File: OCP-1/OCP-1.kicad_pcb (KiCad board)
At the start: 2 copper layers, 45 x 40 mm, 60 parts, among them K1 кнопка, K2 Кнопка_KLS7-TS5401-1.35-250-T, K3 кнопка, K4 кнопка, K5 кнопка, X1 Клеммник_х2

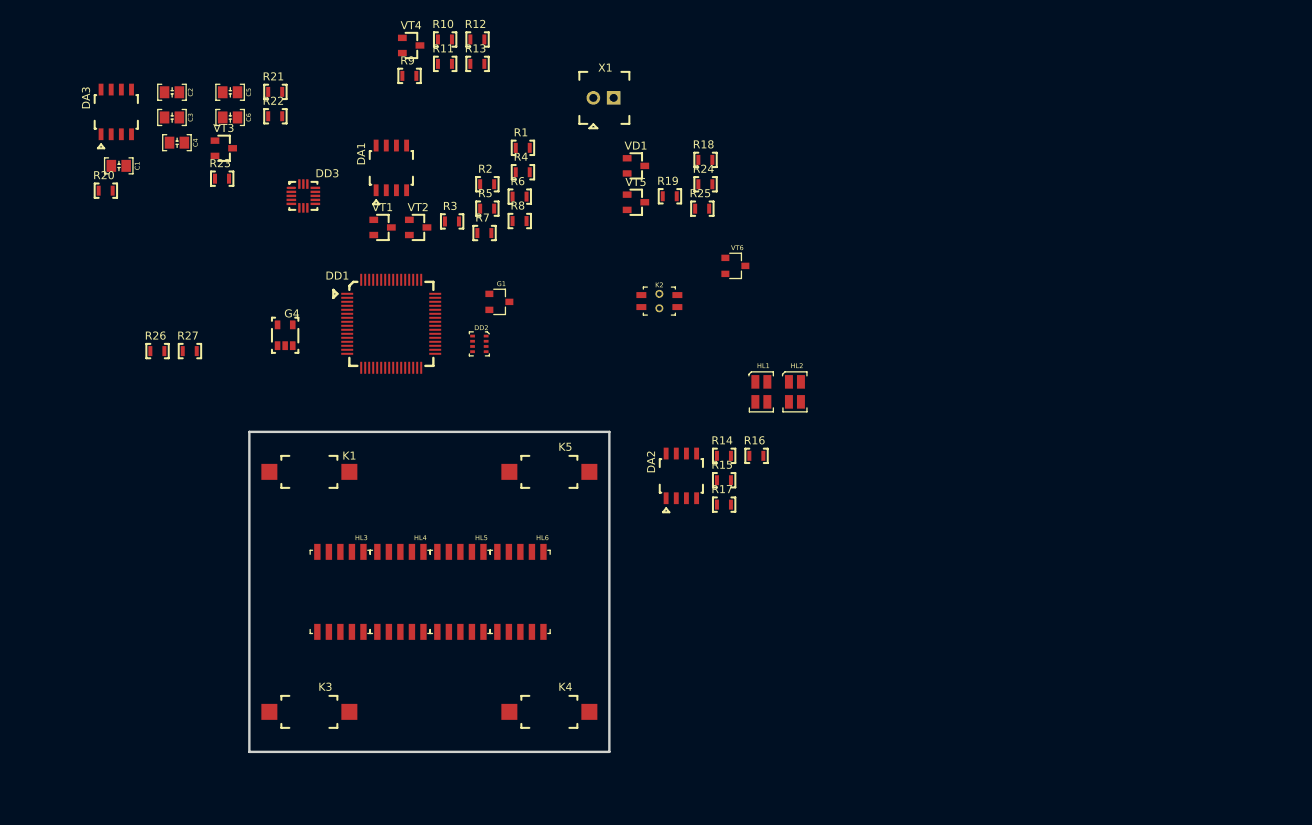
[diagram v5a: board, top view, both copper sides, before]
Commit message: определена схема индикаторов, динамика, не исправлены резисторы питания
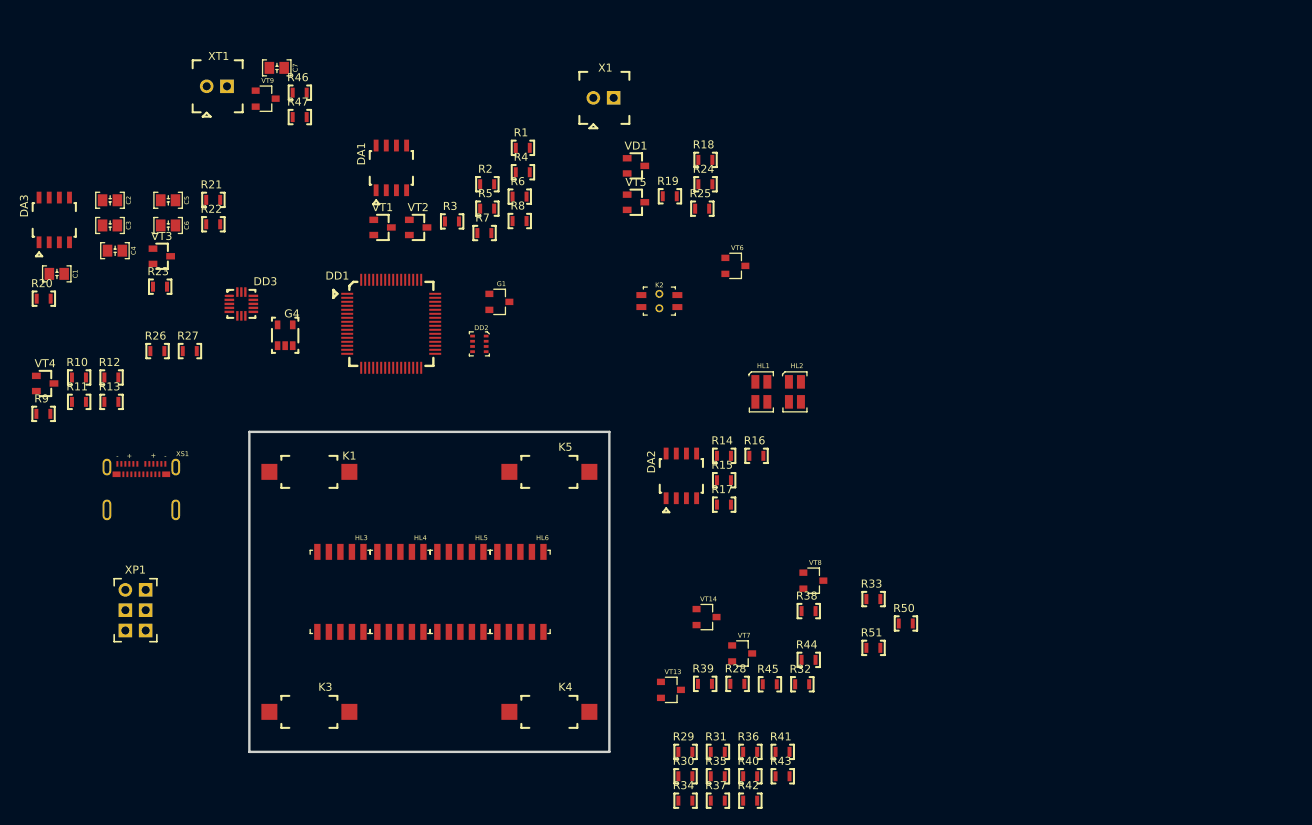
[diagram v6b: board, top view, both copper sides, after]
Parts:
- added C7: Конденсатор_керамический, N_RLC:Конденсатор_SMD_IEC_0805, F.Cu at (77.5, 54.5)
- added R28: Резистор_0,065Вт, N_RLC:Резистор_SMD_0603_0,065_Вт, F.Cu at (136.0, 131.5)
- added R29: Резистор_0,065Вт, N_RLC:Резистор_SMD_0603_0,065_Вт, F.Cu at (129.5, 140.0)
- added R30: Резистор_0,065Вт, N_RLC:Резистор_SMD_0603_0,065_Вт, F.Cu at (129.5, 143.1)
- added R31: Резистор_0,065Вт, N_RLC:Резистор_SMD_0603_0,065_Вт, F.Cu at (133.6, 140.0)
- added R32: Резистор_0,065Вт, N_RLC:Резистор_SMD_0603_0,065_Вт, F.Cu at (144.1, 131.6)
- added R33: Резистор_0,065Вт, N_RLC:Резистор_SMD_0603_0,065_Вт, F.Cu at (153.0, 120.9)
- added R34: Резистор_0,065Вт, N_RLC:Резистор_SMD_0603_0,065_Вт, F.Cu at (129.5, 146.1)
- added R35: Резистор_0,065Вт, N_RLC:Резистор_SMD_0603_0,065_Вт, F.Cu at (133.6, 143.1)
- added R36: Резистор_0,065Вт, N_RLC:Резистор_SMD_0603_0,065_Вт, F.Cu at (137.6, 140.0)
- added R37: Резистор_0,065Вт, N_RLC:Резистор_SMD_0603_0,065_Вт, F.Cu at (133.6, 146.1)
- added R38: Резистор_0,065Вт, N_RLC:Резистор_SMD_0603_0,065_Вт, F.Cu at (144.9, 122.4)
- added R39: Резистор_0,065Вт, N_RLC:Резистор_SMD_0603_0,065_Вт, F.Cu at (131.9, 131.5)
- added R40: Резистор_0,065Вт, N_RLC:Резистор_SMD_0603_0,065_Вт, F.Cu at (137.6, 143.1)
- added R41: Резистор_0,065Вт, N_RLC:Резистор_SMD_0603_0,065_Вт, F.Cu at (141.7, 140.0)
- added R42: Резистор_0,065Вт, N_RLC:Резистор_SMD_0603_0,065_Вт, F.Cu at (137.6, 146.1)
- added R43: Резистор_0,065Вт, N_RLC:Резистор_SMD_0603_0,065_Вт, F.Cu at (141.7, 143.1)
- added R44: Резистор_0,065Вт, N_RLC:Резистор_SMD_0603_0,065_Вт, F.Cu at (144.9, 128.5)
- added R45: Резистор_0,065Вт, N_RLC:Резистор_SMD_0603_0,065_Вт, F.Cu at (140.1, 131.6)
- added R46: Резистор_0,065Вт, N_RLC:Резистор_SMD_0603_0,065_Вт, F.Cu at (81.3, 57.6)
- added R47: Резистор_0,065Вт, N_RLC:Резистор_SMD_0603_0,065_Вт, F.Cu at (81.3, 60.6)
- added R50: Резистор_0,065Вт, N_RLC:Резистор_SMD_0603_0,065_Вт, F.Cu at (157.1, 124.0)
- added R51: Резистор_0,065Вт, N_RLC:Резистор_SMD_0603_0,065_Вт, F.Cu at (153.0, 127.0)
- added VT13: Транзистор_полевой_N-канальный_КП526А9, MOTOR_VD_VT_HL:Корпус_КТ-46, F.Cu at (127.7, 132.2)
- added VT14: Транзистор_полевой_N-канальный_КП526А9, MOTOR_VD_VT_HL:Корпус_КТ-46, F.Cu at (132.1, 123.2)
- added VT7: Транзистор_полевой_N-канальный_КП526А9, MOTOR_VD_VT_HL:Корпус_КТ-46, F.Cu at (136.6, 127.7)
- added VT8: Транзистор_полевой_N-канальный_КП526А9, MOTOR_VD_VT_HL:Корпус_КТ-46, F.Cu at (145.5, 118.6)
- added VT9: Транзистор_полевой_N-канальный_КП526А9, MOTOR_VD_VT_HL:Корпус_КТ-46, F.Cu at (77.0, 58.4)
- added XP1: СНП346-6ВП_(отладочная), MOTOR_X:Вилка_СНП346_6, F.Cu at (59.5, 119.8)
- added XS1: UBS-type-C-105450-0101&упрощенная, N_X:usb-type-c, F.Cu at (58.5, 104.0)
- added XТ1: Клеммник_х2, N_X:Клеммник_х2_шаг2.54, F.Cu at (69.7, 56.8)
- moved R10 62.3 mm to (53.7, 93.2)
- moved R11 62.3 mm to (53.7, 96.2)
- moved R12 62.3 mm to (57.8, 93.2)
- moved R13 62.3 mm to (57.8, 96.2)
- moved R9 62.3 mm to (49.2, 97.8)
- moved VT4 62.3 mm to (49.5, 94.0)
- moved DA3 15.6 mm to (50.6, 73.5)
- moved C2 15.6 mm to (56.6, 71.0)
- moved C3 15.6 mm to (56.6, 74.2)
- moved C1 15.6 mm to (50.0, 80.2)
- moved C5 15.6 mm to (63.9, 71.0)
- moved C6 15.6 mm to (63.9, 74.2)
- moved DD3 15.6 mm to (74.0, 84.0)
- moved R20 15.6 mm to (49.3, 83.3)
- moved R21 15.6 mm to (70.5, 71.0)
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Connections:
- net Net-(R20-Pad1) renamed /V.BATT
- DA1 pad 2: (no net) -> /1V225.REF
- DA1 pad 3: /1V5.FB1 -> /BAT.1V5.FB1
- DA1 pad 6: (no net) -> /1V5.REF
- DA3 pad 5: (no net) -> Net-(DA3-Pad5)
- DA3 pad 6: (no net) -> Net-(DA3-Pad6)
- DA3 pad 7: (no net) -> Net-(DA3-Pad7)
- DD1 pad 1: (no net) -> /3V1
- DD1 pad 10: (no net) -> /USBD-
- DD1 pad 11: (no net) -> /GND
- DD1 pad 12: (no net) -> /3V1
- DD1 pad 13: (no net) -> /3V1
- DD1 pad 14: (no net) -> Net-(DD1-Pad14)
- DD1 pad 15: (no net) -> Net-(DD1-Pad15)
- DD1 pad 16: (no net) -> Net-(DD1-Pad16)
- DD1 pad 17: (no net) -> Net-(DD1-Pad17)
- DD1 pad 18: (no net) -> /RES
- DD1 pad 19: (no net) -> Net-(DD1-Pad19)
- DD1 pad 2: (no net) -> Net-(DD1-Pad2)
- DD1 pad 20: (no net) -> Net-(DD1-Pad20)
- DD1 pad 21: (no net) -> Net-(DD1-Pad21)
- DD1 pad 22: (no net) -> Net-(DD1-Pad22)
- DD1 pad 23: (no net) -> /GND
- DD1 pad 24: (no net) -> /3V1
- DD1 pad 25: (no net) -> Net-(DD1-Pad25)
- DD1 pad 26: (no net) -> Net-(DD1-Pad26)
- DD1 pad 27: (no net) -> /GND
- DD1 pad 28: (no net) -> /3V1
- DD1 pad 29: (no net) -> /DIFF.AMP
- DD1 pad 3: (no net) -> Net-(DD1-Pad3)
- DD1 pad 30: (no net) -> Net-(DD1-Pad30)
- DD1 pad 31: (no net) -> /TMS
- DD1 pad 32: (no net) -> /TCK
- DD1 pad 33: (no net) -> Net-(DD1-Pad33)
- DD1 pad 34: (no net) -> Net-(DD1-Pad34)
- DD1 pad 35: (no net) -> Net-(DD1-Pad35)
- DD1 pad 36: (no net) -> /BAT.1V5.FB1
- DD1 pad 37: (no net) -> Net-(DD1-Pad37)
- DD1 pad 38: (no net) -> /3V1
- DD1 pad 39: (no net) -> /GND
- DD1 pad 4: (no net) -> Net-(DD1-Pad4)
- DD1 pad 40: (no net) -> Net-(DD1-Pad40)
- DD1 pad 41: (no net) -> /SDA
- DD1 pad 42: (no net) -> /SCL
- DD1 pad 43: (no net) -> Net-(DD1-Pad43)
- DD1 pad 44: (no net) -> Net-(DD1-Pad44)
- DD1 pad 45: (no net) -> Net-(DD1-Pad45)
- DD1 pad 46: (no net) -> Net-(DD1-Pad46)
- DD1 pad 47: (no net) -> Net-(DD1-Pad47)
- DD1 pad 48: (no net) -> /3V1
- DD1 pad 49: (no net) -> /GND
- DD1 pad 5: (no net) -> Net-(DD1-Pad5)
- DD1 pad 50: (no net) -> Net-(DD1-Pad50)
- DD1 pad 51: (no net) -> Net-(DD1-Pad51)
- DD1 pad 52: (no net) -> /T3C4
- DD1 pad 53: (no net) -> Net-(DD1-Pad53)
- DD1 pad 54: (no net) -> Net-(DD1-Pad54)
- DD1 pad 55: (no net) -> Net-(DD1-Pad55)
- DD1 pad 56: (no net) -> /DP
- DD1 pad 57: (no net) -> /G
- DD1 pad 58: (no net) -> /F
- DD1 pad 59: (no net) -> /E
- DD1 pad 6: (no net) -> Net-(DD1-Pad6)
- DD1 pad 60: (no net) -> /D
- DD1 pad 61: (no net) -> /C
- DD1 pad 62: (no net) -> /B
- DD1 pad 63: (no net) -> /A
- DD1 pad 64: (no net) -> /GND
- DD1 pad 7: (no net) -> Net-(DD1-Pad7)
- DD1 pad 8: (no net) -> Net-(DD1-Pad8)
- DD1 pad 9: (no net) -> /USBD+
- DD2 pad 1: (no net) -> Net-(DD2-Pad1)
- DD2 pad 2: (no net) -> Net-(DD2-Pad2)
- DD2 pad 3: (no net) -> Net-(DD2-Pad3)
- DD2 pad 4: (no net) -> Net-(DD2-Pad4)
- DD2 pad 5: (no net) -> Net-(DD2-Pad5)
- DD2 pad 6: (no net) -> Net-(DD2-Pad6)
- DD2 pad 7: (no net) -> Net-(DD2-Pad7)
- DD2 pad 8: (no net) -> Net-(DD2-Pad8)
- DD3 pad 1: (no net) -> Net-(DD3-Pad1)
- DD3 pad 10: (no net) -> Net-(DD3-Pad10)
- DD3 pad 11: (no net) -> Net-(DD3-Pad11)
- DD3 pad 12: (no net) -> Net-(DD3-Pad12)
- DD3 pad 13: (no net) -> Net-(DD3-Pad13)
- DD3 pad 14: (no net) -> Net-(DD3-Pad14)
- DD3 pad 15: (no net) -> Net-(DD3-Pad15)
- DD3 pad 16: (no net) -> Net-(DD3-Pad16)
- DD3 pad 2: (no net) -> Net-(DD3-Pad2)
- DD3 pad 3: (no net) -> Net-(DD3-Pad3)
- DD3 pad 4: (no net) -> Net-(DD3-Pad4)
- DD3 pad 5: (no net) -> Net-(DD3-Pad5)
- DD3 pad 6: (no net) -> Net-(DD3-Pad6)
- DD3 pad 7: (no net) -> Net-(DD3-Pad7)
- DD3 pad 8: (no net) -> Net-(DD3-Pad8)
- DD3 pad 9: (no net) -> Net-(DD3-Pad9)
- G1 pad 3: (no net) -> Net-(G1-Pad3)
- G4 pad 4: (no net) -> Net-(G4-Pad4)
- HL1 pad 1: (no net) -> Net-(HL1-Pad1)
- HL1 pad 2: (no net) -> Net-(HL1-Pad2)
- HL1 pad 3: (no net) -> Net-(HL1-Pad3)
- HL1 pad 4: (no net) -> Net-(HL1-Pad4)
- HL2 pad 1: (no net) -> Net-(HL2-Pad1)
- HL2 pad 2: (no net) -> Net-(HL2-Pad2)
- HL2 pad 3: (no net) -> Net-(HL2-Pad3)
- HL2 pad 4: (no net) -> Net-(HL2-Pad4)
- HL3 pad 1: (no net) -> /HL.E
- HL3 pad 10: (no net) -> /HL.G
- HL3 pad 2: (no net) -> /HL.D
- HL3 pad 3: (no net) -> /HL1.C
- HL3 pad 4: (no net) -> /HL.C
- HL3 pad 5: (no net) -> /HL.DP
- HL3 pad 6: (no net) -> /HL.B
- HL3 pad 7: (no net) -> /HL.A
- HL3 pad 8: (no net) -> /HL1.C
- HL3 pad 9: (no net) -> /HL.F
- HL4 pad 1: (no net) -> /HL.E
- HL4 pad 10: (no net) -> /HL.G
- HL4 pad 2: (no net) -> /HL.D
- HL4 pad 3: (no net) -> /HL2.C
- HL4 pad 4: (no net) -> /HL.C
- HL4 pad 5: (no net) -> /HL.DP
- HL4 pad 6: (no net) -> /HL.B
- HL4 pad 7: (no net) -> /HL.A
- HL4 pad 8: (no net) -> /HL2.C
- HL4 pad 9: (no net) -> /HL.F
- HL5 pad 1: (no net) -> /HL.E
- HL5 pad 10: (no net) -> /HL.G
- HL5 pad 2: (no net) -> /HL.D
- HL5 pad 3: (no net) -> /HL3.C
- HL5 pad 4: (no net) -> /HL.C
- HL5 pad 5: (no net) -> /HL.DP
- HL5 pad 6: (no net) -> /HL.B
- HL5 pad 7: (no net) -> /HL.A
- HL5 pad 8: (no net) -> /HL3.C
- HL5 pad 9: (no net) -> /HL.F
- HL6 pad 1: (no net) -> /HL.E
- HL6 pad 10: (no net) -> /HL.G
- HL6 pad 2: (no net) -> /HL.D
- HL6 pad 3: (no net) -> /HL4.C
- HL6 pad 4: (no net) -> /HL.C
- HL6 pad 5: (no net) -> /HL.DP
- HL6 pad 6: (no net) -> /HL.B
- HL6 pad 7: (no net) -> /HL.A
- HL6 pad 8: (no net) -> /HL4.C
- HL6 pad 9: (no net) -> /HL.F
- K1 pad 2: (no net) -> Net-(K1-Pad2)
- K3 pad 2: (no net) -> Net-(K3-Pad2)
- K4 pad 2: (no net) -> Net-(K4-Pad2)
- K5 pad 2: /B-PWR -> Net-(K5-Pad2)
- R12 pad 2: /1V5.FB1 -> /BAT.1V5.FB1
- R13 pad 1: /1V5.FB1 -> /BAT.1V5.FB1
- R24 pad 1: (no net) -> /SELF-TURN
- R25 pad 1: (no net) -> /SENS-B-PWR
- VT1 pad 3: (no net) -> /5V.IN
